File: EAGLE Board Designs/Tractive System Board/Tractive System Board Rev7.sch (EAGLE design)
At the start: 116 parts, among them J1 CONNECTOR-5_MICRO_V7S_, J2 CONNECTOR-5_MICRO_V6S_, J3 CONNECTOR-8_μF_T_V_BLACK, K1 RELAY_SPST_NO_D_24, Q1 TRANSISTOR_N_MOS_POWERFLAT5X6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, Q2 TRANSISTOR_N_MOS__PMV15ENEA, T1 TRANSFORMER(3W), U1 VOLTAGE_REGULATOR_SOT-223_10V, U10 LTC6994-2, U2 LT8316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

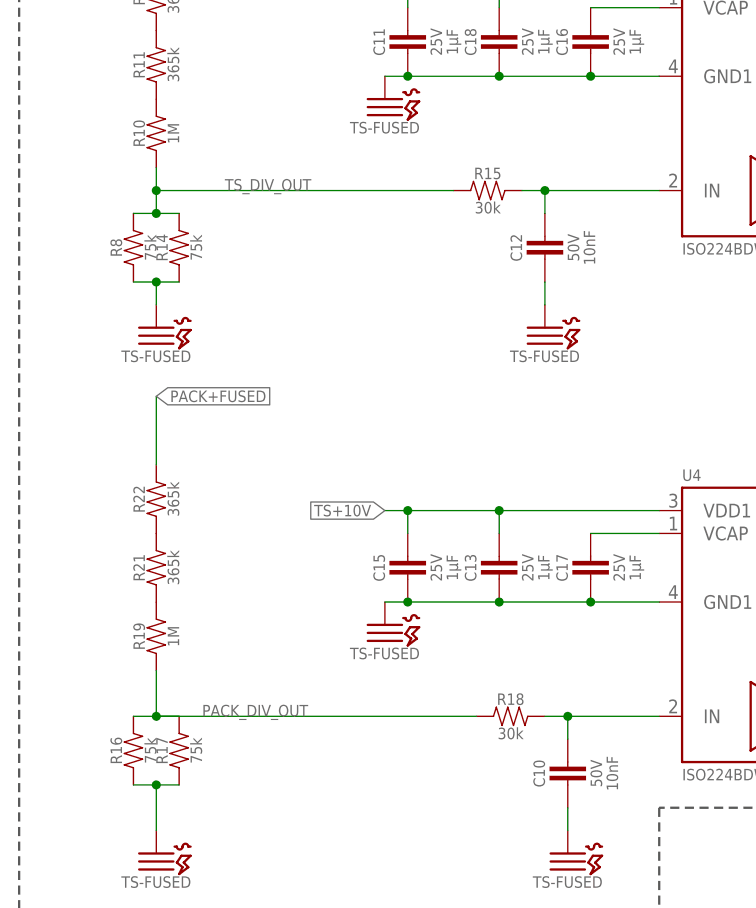
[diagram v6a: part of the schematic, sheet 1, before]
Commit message: tsb-rev7 update
Get rid of R15 & R18 (Didn't account for Thevenin resistance of the resistor divider)
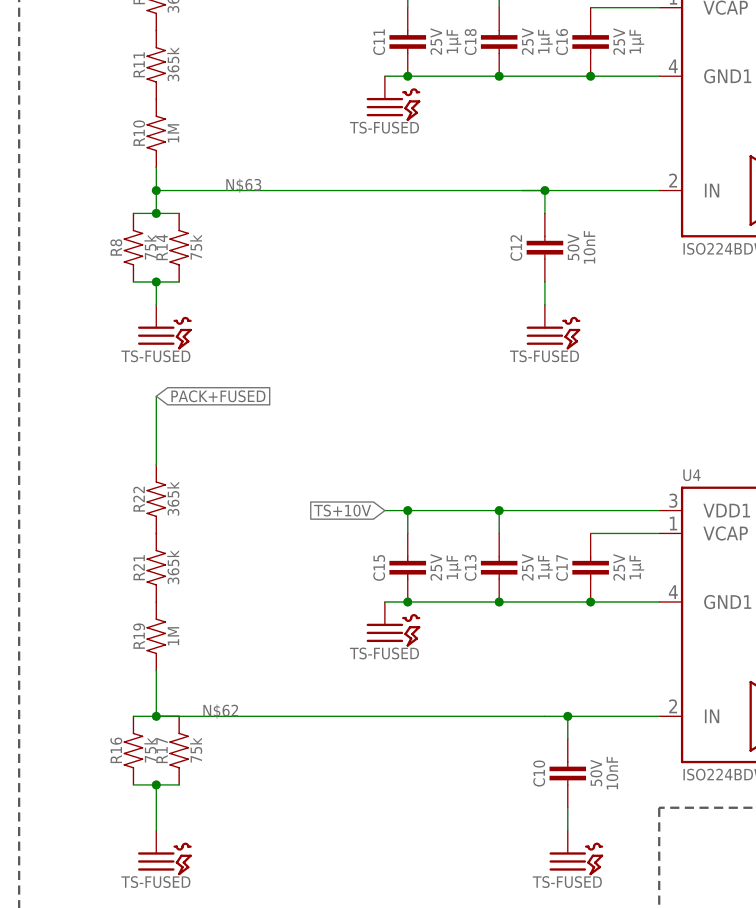
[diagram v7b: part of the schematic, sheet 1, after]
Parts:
- removed R15, R18: RESISTOR_0603_, HyTechDevices:RESISTOR_0603_30K
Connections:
- net N$62: now also R16.2, R17.2, R19.1; no longer R18.2
- net N$63: now also R10.1, R14.2, R8.2; no longer R15.2
- net PACK_DIV_OUT: no longer R16.2, R17.2, R18.1, R19.1
- net TS_DIV_OUT: no longer R10.1, R14.2, R15.1, R8.2
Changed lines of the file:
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@@
 <part name="P47" library="HyTechSupplies" deviceset="GND" device=""/>
 <part name="P48" library="HyTechSupplies" deviceset="GND" device=""/>
-<part name="R18" library="HyTechDevices" deviceset="RESISTOR_?_*" device="0603" technology="30K" value="RESISTOR_0603_"/>
-<part name="R15" library="HyTechDevices" deviceset="RESISTOR_?_*" device="0603" technology="30K" value="RESISTOR_0603_"/>
 <part name="C10" library="HyTechDevices" deviceset="CAPACITOR_?_*" device="0603" technology="50V_10NF" value="CAPACITOR_0603_50V_10NF"/>
 <part name="C12" library="HyTechDevices" deviceset="CAPACITOR_?_*" device="0603" technology="50V_10NF" value="CAPACITOR_0603_50V_10NF"/>
@@
 <attribute name="VALUE" x="121.92" y="41.91" size="1.27" layer="96" align="top-center"/>
 </instance>
-<instance part="R18" gate="G$1" x="60.96" y="33.02" smashed="yes">
-<attribute name="NAME" x="59.69" y="34.29" size="1.27" layer="95" align="bottom-center"/>
-<attribute name="RESISTANCE" x="59.69" y="31.75" size="1.27" layer="96" align="top-center"/>
-</instance>
-<instance part="R15" gate="G$1" x="58.42" y="91.44" smashed="yes">
-<attribute name="NAME" x="57.15" y="92.71" size="1.27" layer="95" align="bottom-center"/>
-<attribute name="RESISTANCE" x="57.15" y="90.17" size="1.27" layer="96" align="top-center"/>
-</instance>
 <instance part="C10" gate="G$1" x="66.04" y="27.94" smashed="yes" rot="R90">
 <attribute name="NAME" x="63.5" y="26.67" size="1.27" layer="95" rot="R90" align="bottom-center"/>
@@
 <net name="N$62" class="0">
 <segment>
-<pinref part="R18" gate="G$1" pin="2"/>
 <pinref part="C10" gate="G$1" pin="1"/>
 <wire x1="63.5" y1="33.02" x2="66.04" y2="33.02" width="0.6096" layer="91"/>
@@
 <wire x1="66.04" y1="33.02" x2="76.2" y2="33.02" width="0.6096" layer="91"/>
 <junction x="66.04" y="33.02"/>
-</segment>
-</net>
-<net name="N$63" class="0">
-<segment>
-<pinref part="R15" gate="G$1" pin="2"/>
-<pinref part="C12" gate="G$1" pin="1"/>
-<wire x1="60.96" y1="91.44" x2="63.5" y2="91.44" width="0.6096" layer="91"/>
-<wire x1="63.5" y1="91.44" x2="63.5" y2="88.9" width="0.6096" layer="91"/>
-<pinref part="U3" gate="G$1" pin="IN"/>
-<wire x1="63.5" y1="91.44" x2="76.2" y2="91.44" width="0.6096" layer="91"/>
-<junction x="63.5" y="91.44"/>
-</segment>
-</net>
-<net name="PACK_DIV_OUT" class="0">
-<segment>
-<pinref part="R18" gate="G$1" pin="1"/>
-<wire x1="20.32" y1="33.02" x2="55.88" y2="33.02" width="0.6096" layer="91"/>
+<wire x1="20.32" y1="33.02" x2="63.5" y2="33.02" width="0.6096" layer="91"/>
 <label x="25.4" y="33.02" size="1.27" layer="95"/>
 <wire x1="17.78" y1="33.02" x2="20.32" y2="33.02" width="0.6096" layer="91"/>
@@
 <pinref part="R19" gate="G$1" pin="1"/>
 </segment>
-<segment>
-<pinref part="PACK_DIV_OUT" gate="G$1" pin="1"/>
-<wire x1="20.32" y1="132.08" x2="22.86" y2="132.08" width="0.1524" layer="91"/>
-<label x="22.86" y="132.08" size="1.27" layer="95" xref="yes"/>
-</segment>
-</net>
-<net name="TS_DIV_OUT" class="0">
-<segment>
+</net>
+<net name="N$63" class="0">
+<segment>
+<pinref part="C12" gate="G$1" pin="1"/>
+<wire x1="60.96" y1="91.44" x2="63.5" y2="91.44" width="0.6096" layer="91"/>
+<wire x1="63.5" y1="91.44" x2="63.5" y2="88.9" width="0.6096" layer="91"/>
+<pinref part="U3" gate="G$1" pin="IN"/>
+<wire x1="63.5" y1="91.44" x2="76.2" y2="91.44" width="0.6096" layer="91"/>
+<junction x="63.5" y="91.44"/>
 <wire x1="17.78" y1="88.9" x2="20.32" y2="88.9" width="0.6096" layer="91"/>
-<pinref part="R15" gate="G$1" pin="1"/>
 <wire x1="20.32" y1="88.9" x2="22.86" y2="88.9" width="0.6096" layer="91"/>
-<wire x1="20.32" y1="91.44" x2="53.34" y2="91.44" width="0.6096" layer="91"/>
+<wire x1="20.32" y1="91.44" x2="63.5" y2="91.44" width="0.6096" layer="91"/>
 <wire x1="20.32" y1="88.9" x2="20.32" y2="91.44" width="0.6096" layer="91"/>
 <junction x="20.32" y="88.9"/>
@@
 <pinref part="R10" gate="G$1" pin="1"/>
 </segment>
+</net>
+<net name="PACK_DIV_OUT" class="0">
+<segment>
+<pinref part="PACK_DIV_OUT" gate="G$1" pin="1"/>
+<wire x1="20.32" y1="132.08" x2="22.86" y2="132.08" width="0.1524" layer="91"/>
+<label x="22.86" y="132.08" size="1.27" layer="95" xref="yes"/>
+</segment>
+</net>
+<net name="TS_DIV_OUT" class="0">
 <segment>
 <pinref part="TS_DIV_OUT" gate="G$1" pin="1"/>

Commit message: Update Tractive System Board Rev7.sch
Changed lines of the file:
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@@
 <part name="R38" library="HyTechDevices" deviceset="RESISTOR_?_*" device="1206" technology="HV46.4K"/>
 <part name="C29" library="HyTechDevices" deviceset="CAPACITOR_?_*" device="1812" technology="1000V_0.1UF"/>
+<part name="FRAME1" library="HyTechFrames" deviceset="FRAME" device="">
+<attribute name="DESCRIPTION_1" value="Precharge power stage"/>
+<attribute name="DESIGNER_BOARD" value="Liwei Sun"/>
+<attribute name="DESIGNER_SCHEMATIC" value="Liwei Sun"/>
+<attribute name="ENGINEER" value="Liwei Sun"/>
+</part>
 </parts>
 <sheets>
 <sheet>
 <plain>
+</plain>
+<instances>
+<instance part="FRAME1" gate="O" x="0" y="0" smashed="yes">
+<attribute name="LAST_DATE_TIME" x="186.69" y="2.54" size="2.54" layer="95"/>
+<attribute name="DRAWING_NAME" x="207.01" y="22.86" size="2.54" layer="95"/>
+<attribute name="SHEET" x="259.08" y="2.54" size="2.54" layer="95"/>
+<attribute name="ENGINEER" x="129.54" y="22.86" size="2.54" layer="95"/>
+<attribute name="DESIGNER_SCHEMATIC" x="176.53" y="45.72" size="2.54" layer="95"/>
+<attribute name="DESIGNER_BOARD" x="176.53" y="38.1" size="2.54" layer="95"/>
+<attribute name="DESIGNER_FURTHER" x="176.53" y="30.48" size="2.54" layer="95"/>
+<attribute name="REVIEWER_SCHEMATIC" x="227.33" y="45.72" size="2.54" layer="95"/>
+<attribute name="REVIEWER_BOARD" x="227.33" y="38.1" size="2.54" layer="95"/>
+<attribute name="REVIEWER_FURTHER" x="227.33" y="30.48" size="2.54" layer="95"/>
+<attribute name="DESCRIPTION_1" x="196.85" y="15.24" size="2.54" layer="95"/>
+<attribute name="DESCRIPTION_2" x="176.53" y="10.16" size="2.54" layer="95"/>
+</instance>
+</instances>
+<busses>
+</busses>
+<nets>
+</nets>
+</sheet>
+<sheet>
+<plain>
